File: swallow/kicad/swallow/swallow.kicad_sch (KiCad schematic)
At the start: 0 parts

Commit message: ++ - kamangir/bolt#746
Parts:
- added C1: 470 mF, symbol Device:C
- added D1: yellow, symbol Device:LED
- added D2: red, symbol Device:LED
- added D3: green, symbol Device:LED
- added D4: P6KE6.8A, Diode_SMD:D_SOD-523, symbol Diode:1N4148WT
- added D5, D6, D7, D8: blue, symbol Device:LED
- added J1: Raspberry_Pi_2_3, symbol Connector:Raspberry_Pi_2_3
- added J2: echo2, symbol Connector:Conn_01x01_Pin
- added J3: ground, symbol Connector_Generic:Conn_02x06_Top_Bottom
- added J4: VCC, symbol Connector_Generic:Conn_02x06_Top_Bottom
- added J5: echo3, symbol Connector:Conn_01x01_Pin
- added J6: echo4, symbol Connector:Conn_01x01_Pin
- added J7: echo1, symbol Connector:Conn_01x01_Pin
- added J8: power terminal, symbol Connector:Screw_Terminal_01x02
- added R1, R11, R14, R2, R3, R6, R8: 330 ohm, symbol Device:R
- added R10, R13, R5, R7: 3.3 kohm, symbol Device:R
- added R12, R15, R4, R9: 2.2 kohm, symbol Device:R
- added SW1: SW_Push, symbol Switch:SW_Push
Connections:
- new net: D6.1 (K), R8.1
- new net: C1.2, D1.1 (K), D2.1 (K), D3.1 (K), D4.1 (K), J1.14 (GND), J1.20 (GND), J1.25 (GND), J1.30 (GND), J1.34 (GND), J1.39 (GND), J1.6 (GND), J1.9 (GND), J3.1 (Pin_1), J3.10 (Pin_10), J3.11 (Pin_11), J3.12 (Pin_12), J3.2 (Pin_2), J3.3 (Pin_3), J3.4 (Pin_4), J3.5 (Pin_5), J3.6 (Pin_6), J3.7 (Pin_7), J3.8 (Pin_8), J3.9 (Pin_9), J8.1 (Pin_1), R10.2, R11.2, R13.2, R14.2, R5.2, R6.2, R7.2, R8.2, SW1.1
- new net: C1.1, D4.2 (A), J1.2 (5V), J1.4 (5V), J4.1 (Pin_1), J4.10 (Pin_10), J4.11 (Pin_11), J4.12 (Pin_12), J4.2 (Pin_2), J4.3 (Pin_3), J4.4 (Pin_4), J4.5 (Pin_5), J4.6 (Pin_6), J4.7 (Pin_7), J4.9 (Pin_9), J8.2 (Pin_2)
- new net: D6.2 (A), J1.38 (GPIO20/MOSI1), R7.1, R9.2
- new net: J7.1 (Pin_1), R15.1
- new net: D8.2 (A), J1.18 (GPIO24), R13.1, R15.2
- new net: D3.2 (A), R3.1
- new net: D8.1 (K), R14.1
- new net: J6.1 (Pin_1), R12.1
- new net: D7.2 (A), J1.40 (GPIO21/SCLK1), R10.1, R12.2
- new net: D7.1 (K), R11.1
- new net: D1.2 (A), R1.1
- new net: J1.11 (GPIO17), R1.2
- new net: J5.1 (Pin_1), R9.1
- new net: D5.2 (A), J1.22 (GPIO25), R4.2, R5.1
- new net: D2.2 (A), R2.1
- new net: D5.1 (K), R6.1
- new net: J1.13 (GPIO27), R3.2
- new net: J2.1 (Pin_1), R4.1
- new net: J1.15 (GPIO22), R2.2
- new net: J1.37 (GPIO26), SW1.2
- new net: J1.1 (3V3), J1.17 (3V3)

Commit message: ++ - kamangir/bolt#746
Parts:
- added J10: evens, symbol Connector:Conn_01x20_Pin
- added J9: odds, symbol Connector:Conn_01x20_Pin
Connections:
- net at J1.12 (GPIO18/PWM0): now also J10.6 (Pin_6)
- net at J1.16 (GPIO23): now also J10.8 (Pin_8)
- net at J1.29 (GCLK1/GPIO5): now also J9.15 (Pin_15)
- net at J1.31 (GCLK2/GPIO6): now also J9.16 (Pin_16)
- net at J1.32 (PWM0/GPIO12): now also J10.16 (Pin_16)
- net at J1.33 (PWM1/GPIO13): now also J9.17 (Pin_17)
- net at J1.35 (GPIO19/MISO1): now also J9.18 (Pin_18)
- net at J1.36 (GPIO16): now also J10.18 (Pin_18)
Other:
- moved on the sheet: C1, D4, J8

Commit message: ++ - kamangir/bolt#746
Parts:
- C1: value 470 mF -> 470 µF; footprint (none) -> Capacitor_THT:CP_Radial_D8.0mm_P3.50mm
- D1, D5, D6, D7, D8: footprint (none) -> LED_THT:LED_D5.0mm
- D2: renamed from D3; value green -> red; footprint (none) -> LED_THT:LED_D5.0mm
- D3: renamed from D2; value red -> green; footprint (none) -> LED_THT:LED_D5.0mm
- D4: footprint Diode_SMD:D_SOD-523 -> Diode_THT:D_DO-15_P10.16mm_Horizontal
- J1: footprint (none) -> Connector_PinHeader_2.54mm:PinHeader_2x20_P2.54mm_Vertical
- J10, J9: footprint (none) -> Connector_PinHeader_2.54mm:PinHeader_1x20_P2.54mm_Vertical
- J2, J5, J6, J7: footprint (none) -> Connector_PinHeader_2.54mm:PinHeader_1x01_P2.54mm_Vertical
- J3, J4: footprint (none) -> Connector_PinHeader_2.54mm:PinHeader_2x04_P2.54mm_Vertical
- J8: footprint (none) -> TerminalBlock:TerminalBlock_MaiXu_MX126-5.0-02P_1x02_P5.00mm
- R1, R10, R11, R12, R13, R14, R15, R4, R5, R6, R7, R8, R9: footprint (none) -> Resistor_THT:R_Axial_DIN0207_L6.3mm_D2.5mm_P10.16mm_Horizontal
- R2: renamed from R3; footprint (none) -> Resistor_THT:R_Axial_DIN0207_L6.3mm_D2.5mm_P10.16mm_Horizontal
- R3: renamed from R2; footprint (none) -> Resistor_THT:R_Axial_DIN0207_L6.3mm_D2.5mm_P10.16mm_Horizontal
- SW1: footprint (none) -> Button_Switch_THT:SW_PUSH_6mm
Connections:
- net at R8.1: now also D6.2 (A); no longer D6.1 (K)
- net at C1.2, D1.1 (K), D2.1 (K)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: now also D5.1 (K), D6.1 (K), D7.1 (K), D8.1 (K), J1.13 (GPIO27), J9.7 (Pin_7), R2.2; no longer R11.2, R14.2, R6.2, R8.2
- net at C1.1, D4.2 (A), J1.2 (5V)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: now also J1.11 (GPIO17), J4.8 (Pin_8), J9.6 (Pin_6), R1.2
- net at J1.38 (GPIO20/MOSI1), R7.1, R9.2: now also J10.19 (Pin_19), R8.2; no longer D6.2 (A)
- net at J9.19 (Pin_19): now also J1.37 (GPIO26), SW1.2
- net at J9.8 (Pin_8): now also J1.15 (GPIO22), R3.2
- net at J1.18 (GPIO24), R13.1, R15.2: now also J10.9 (Pin_9), R14.2; no longer D8.2 (A)
- net at R14.1: now also D8.2 (A); no longer D8.1 (K)
- net at J1.40 (GPIO21/SCLK1), R10.1, R12.2: now also J10.20 (Pin_20), R11.1; no longer D7.2 (A)
- net at J1.22 (GPIO25), R4.2, R5.1: now also J10.11 (Pin_11), R6.1; no longer D5.2 (A)
- new net: D7.2 (A), R11.2
- new net: D5.2 (A), R6.2
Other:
- moved on the sheet: D5, D6, D7, D8, J5, J6, R10, R11, R12, R14, R6, R7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

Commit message: ++ - kamangir/bolt#746
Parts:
- J1: footprint Connector_PinHeader_2.54mm:PinHeader_2x20_P2.54mm_Vertical -> Connector_PinSocket_2.54mm:PinSocket_2x20_P2.54mm_Vertical
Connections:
- net at C1.1, D4.2 (A), J1.2 (5V)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: now also J10.1 (Pin_1); no longer J1.11 (GPIO17), J9.6 (Pin_6), R1.2
- net at C1.2, D1.1 (K), D2.1 (K)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: now also J10.3 (Pin_3); no longer J1.13 (GPIO27), J9.7 (Pin_7), R2.2
- new net: J1.11 (GPIO17), J9.6 (Pin_6), R1.2
- new net: J1.13 (GPIO27), J9.7 (Pin_7), R2.2
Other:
- moved on the sheet: C1, D4
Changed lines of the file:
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@@
 	)
 	(junction
+		(at 200.66 43.18)
+		(diameter 0)
+		(color 0 0 0 0)
+	)
+	(junction
 		(at 140.97 134.62)
 		(diameter 0)
@@
 	)
 	(junction
-		(at 128.27 43.18)
+		(at 205.74 134.62)
 		(diameter 0)
 		(color 0 0 0 0)
 	)
 	(junction
-		(at 121.92 80.01)
+		(at 128.27 43.18)
 		(diameter 0)
 		(color 0 0 0 0)
 	)
 	(junction
-		(at 143.51 58.42)
+		(at 121.92 80.01)
 		(diameter 0)
 		(color 0 0 0 0)
@@
 	)
 	(junction
-		(at 143.51 66.04)
-		(diameter 0)
-		(color 0 0 0 0)
-	)
-	(junction
 		(at 177.8 43.18)
 		(diameter 0)
@@
 	(wire
 		(pts
-			(xy 128.27 64.77) (xy 128.27 80.01)
+			(xy 128.27 76.2) (xy 128.27 80.01)
 		)
 		(stroke
@@
 	(wire
 		(pts
-			(xy 128.27 43.18) (xy 128.27 57.15)
+			(xy 128.27 43.18) (xy 128.27 68.58)
 		)
 		(stroke
@@
 	(wire
 		(pts
-			(xy 143.51 66.04) (xy 39.37 66.04)
-		)
-		(stroke
-			(width 0)
-			(type default)
-		)
-	)
-	(wire
-		(pts
 			(xy 46.99 49.53) (xy 46.99 114.3)
 		)
@@
 	(wire
 		(pts
-			(xy 143.51 58.42) (xy 38.1 58.42)
-		)
-		(stroke
-			(width 0)
-			(type default)
-		)
-	)
-	(wire
-		(pts
 			(xy 140.97 157.48) (xy 140.97 134.62)
 		)
@@
 	(wire
 		(pts
+			(xy 251.46 72.39) (xy 251.46 43.18)
+		)
+		(stroke
+			(width 0)
+			(type default)
+		)
+	)
+	(wire
+		(pts
 			(xy 71.12 80.01) (xy 76.2 80.01)
 		)
@@
 	(wire
 		(pts
-			(xy 175.26 58.42) (xy 143.51 58.42)
+			(xy 38.1 58.42) (xy 175.26 58.42)
 		)
 		(stroke
@@
 	(wire
 		(pts
+			(xy 246.38 134.62) (xy 205.74 134.62)
+		)
+		(stroke
+			(width 0)
+			(type default)
+		)
+	)
+	(wire
+		(pts
 			(xy 119.38 67.31) (xy 41.91 67.31)
 		)
@@
 	(wire
 		(pts
+			(xy 262.89 77.47) (xy 246.38 77.47)
+		)
+		(stroke
+			(width 0)
+			(type default)
+		)
+	)
+	(wire
+		(pts
 			(xy 121.92 91.44) (xy 121.92 97.79)
 		)
@@
 	(wire
 		(pts
-			(xy 143.51 66.04) (xy 143.51 80.01)
+			(xy 143.51 77.47) (xy 143.51 80.01)
 		)
 		(stroke
@@
 	(wire
 		(pts
-			(xy 173.99 66.04) (xy 143.51 66.04)
+			(xy 246.38 77.47) (xy 246.38 134.62)
+		)
+		(stroke
+			(width 0)
+			(type default)
+		)
+	)
+	(wire
+		(pts
+			(xy 39.37 66.04) (xy 173.99 66.04)
 		)
 		(stroke
@@
 	(wire
 		(pts
+			(xy 262.89 72.39) (xy 251.46 72.39)
+		)
+		(stroke
+			(width 0)
+			(type default)
+		)
+	)
+	(wire
+		(pts
 			(xy 185.42 102.87) (xy 144.78 102.87)
 		)
@@
 	(wire
 		(pts
-			(xy 143.51 43.18) (xy 143.51 58.42)
+			(xy 143.51 43.18) (xy 143.51 69.85)
 		)
 		(stroke
@@
 	(wire
 		(pts
+			(xy 251.46 43.18) (xy 200.66 43.18)
+		)
+		(stroke
+			(width 0)
+			(type default)
+		)
+	)
+	(wire
+		(pts
 			(xy 176.53 114.3) (xy 132.08 114.3)
 		)
@@
 		)
 	)
-	(label "2025-10-09"
-		(at 205.74 194.31 0)
-		(effects
-			(font
-				(size 1.27 1.27)
-			)
-			(justify left bottom)
-		)
-	)
 	(label "swallow shield"
 		(at 186.69 190.5 0)
@@
 		)
 	)
-	(label "v3"
+	(label "v4"
 		(at 267.97 194.31 0)
 		(effects
@@
 	(symbol
 		(lib_id "Diode:1N4148WT")
-		(at 143.51 62.23 90)
+		(at 143.51 73.66 90)
 		(unit 1)
 		(exclude_from_sim no)
@@
 		(fields_autoplaced yes)
 		(property "Reference" "D4"
-			(at 146.05 60.9599 90)
+			(at 146.05 72.3899 90)
 			(effects
 				(font
@@
 		)
 		(property "Value" "P6KE6.8A"
-			(at 146.05 63.4999 90)
+			(at 146.05 74.9299 90)
 			(effects
 				(font
@@
 		)
 		(property "Footprint" "Diode_THT:D_DO-15_P10.16mm_Horizontal"
-			(at 147.955 62.23 0)
+			(at 147.955 73.66 0)
 			(effects
 				(font
@@
 		)
 		(property "Datasheet" "https://www.diodes.com/assets/Datasheets/ds30396.pdf"
-			(at 143.51 62.23 0)
+			(at 143.51 73.66 0)
 			(effects
 				(font
@@
 		)
 		(property "Description" "75V 0.15A Fast switching Diode, SOD-523"
-			(at 143.51 62.23 0)
+			(at 143.51 73.66 0)
 			(effects
 				(font
@@
 		)
 		(property "Sim.Device" "D"
-			(at 143.51 62.23 0)
+			(at 143.51 73.66 0)
 			(effects
 				(font
@@
 		)
 		(property "Sim.Pins" "1=K 2=A"
-			(at 143.51 62.23 0)
+			(at 143.51 73.66 0)
 			(effects
 				(font
@@
 	(symbol
 		(lib_id "Device:C")
-		(at 128.27 60.96 0)
+		(at 128.27 72.39 0)
 		(unit 1)
 		(exclude_from_sim no)
@@
 		(fields_autoplaced yes)
 		(property "Reference" "C1"
-			(at 132.08 59.6899 0)
+			(at 132.08 71.1199 0)
 			(effects
 				(font
@@
 		)
 		(property "Value" "470 µF"
-			(at 132.08 62.2299 0)
+			(at 132.08 73.6599 0)
 			(effects
 				(font
@@
 		)
 		(property "Footprint" "Capacitor_THT:CP_Radial_D8.0mm_P3.50mm"
-			(at 129.2352 64.77 0)
+			(at 129.2352 76.2 0)
 			(effects
 				(font
@@
 		)
 		(property "Datasheet" "~"
-			(at 128.27 60.96 0)
+			(at 128.27 72.39 0)
 			(effects
 				(font
@@
 		)
 		(property "Description" "Unpolarized capacitor"
-			(at 128.27 60.96 0)
+			(at 128.27 72.39 0)
 			(effects
 				(font
@@
 			)
 		)
-		(property "Footprint" "Connector_PinHeader_2.54mm:PinHeader_2x20_P2.54mm_Vertical"
+		(property "Footprint" "Connector_PinSocket_2.54mm:PinSocket_2x20_P2.54mm_Vertical"
 			(at 205.74 92.71 0)
 			(effects

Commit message: ++ - kamangir/bolt#746
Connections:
- net at C1.1, J1.2 (5V), J1.4 (5V)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: now also D4.1 (K); no longer D4.2 (A)
- net at C1.2, D1.1 (K), D2.1 (K)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: now also D4.2 (A), J9.13 (Pin_13); no longer D4.1 (K)
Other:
- moved on the sheet: D4
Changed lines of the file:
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@@
+	)
+	(junction
+		(at 137.16 134.62)
+		(diameter 0)
+		(color 0 0 0 0)
 	)
 	(junction
@@
 	(wire
 		(pts
+			(xy 35.56 106.68) (xy 44.45 106.68)
+		)
+		(stroke
+			(width 0)
+			(type default)
+		)
+	)
+	(wire
+		(pts
 			(xy 251.46 132.08) (xy 251.46 97.79)
 		)
@@
 	(wire
 		(pts
+			(xy 44.45 177.8) (xy 137.16 177.8)
+		)
+		(stroke
+			(width 0)
+			(type default)
+		)
+	)
+	(wire
+		(pts
 			(xy 106.68 148.59) (xy 121.92 148.59)
 		)
@@
 	(wire
 		(pts
+			(xy 44.45 106.68) (xy 44.45 177.8)
+		)
+		(stroke
+			(width 0)
+			(type default)
+		)
+	)
+	(wire
+		(pts
 			(xy 140.97 157.48) (xy 140.97 134.62)
 		)
@@
 	(wire
 		(pts
-			(xy 121.92 134.62) (xy 140.97 134.62)
+			(xy 121.92 134.62) (xy 137.16 134.62)
 		)
 		(stroke
@@
 	(wire
 		(pts
+			(xy 137.16 134.62) (xy 140.97 134.62)
+		)
+		(stroke
+			(width 0)
+			(type default)
+		)
+	)
+	(wire
+		(pts
 			(xy 41.91 93.98) (xy 35.56 93.98)
+		)
+		(stroke
+			(width 0)
+			(type default)
+		)
+	)
+	(wire
+		(pts
+			(xy 137.16 177.8) (xy 137.16 134.62)
 		)
 		(stroke
@@
 	(symbol
 		(lib_id "Diode:1N4148WT")
-		(at 143.51 73.66 90)
+		(at 143.51 73.66 270)
 		(unit 1)
 		(exclude_from_sim no)
@@
 					(size 1.27 1.27)
 				)
-				(justify right)
+				(justify left)
 			)
 		)
@@
 					(size 1.27 1.27)
 				)
-				(justify right)
+				(justify left)
 			)
 		)
 		(property "Footprint" "Diode_THT:D_DO-15_P10.16mm_Horizontal"
-			(at 147.955 73.66 0)
-			(effects
-				(font
+			(at 139.065 73.66 0)
+			(effects
+				(font

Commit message: ++ - kamangir/bolt#746
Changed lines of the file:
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@@
 		)
 	)
-	(label "v4"
+	(label "v14"
 		(at 267.97 194.31 0)
 		(effects

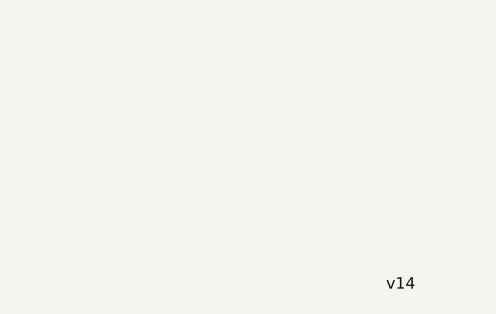
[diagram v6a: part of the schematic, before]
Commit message: fix - kamangir/bolt#746
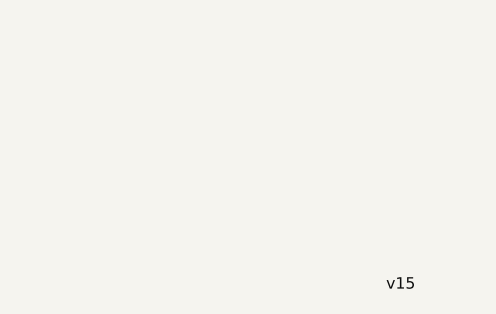
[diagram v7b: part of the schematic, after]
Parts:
- J3, J4: footprint Connector_PinHeader_2.54mm:PinHeader_2x04_P2.54mm_Vertical -> Connector_PinHeader_2.54mm:PinHeader_2x06_P2.54mm_Vertical
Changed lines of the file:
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@@
 		)
 	)
-	(label "v14"
+	(label "v15"
 		(at 267.97 194.31 0)
 		(effects
@@
 			)
 		)
-		(property "Footprint" "Connector_PinHeader_2.54mm:PinHeader_2x04_P2.54mm_Vertical"
+		(property "Footprint" "Connector_PinHeader_2.54mm:PinHeader_2x06_P2.54mm_Vertical"
 			(at 158.75 27.94 0)
 			(effects
@@
 			)
 		)
-		(property "Footprint" "Connector_PinHeader_2.54mm:PinHeader_2x04_P2.54mm_Vertical"
+		(property "Footprint" "Connector_PinHeader_2.54mm:PinHeader_2x06_P2.54mm_Vertical"
 			(at 161.29 149.86 0)
 			(effects

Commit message: ++ - kamangir/bolt#746
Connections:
- net pin2: now reaches C1.1, D4.1 (K), J1.2 (5V), J1.4 (5V), J10.1 (Pin_1), J4.1 (Pin_1), J4.10 (Pin_10), J4.11 (Pin_11), J4.12 (Pin_12), J4.2 (Pin_2), J4.3 (Pin_3), J4.4 (Pin_4), J4.5 (Pin_5), J4.6 (Pin_6), J4.7 (Pin_7), J4.8 (Pin_8), J4.9 (Pin_9), J8.2 (Pin_2)
- net pin2: now also J10.2 (Pin_2)
- net pin14: now reaches C1.2, D1.1 (K), D2.1 (K), D3.1 (K), D4.2 (A), D5.1 (K), D6.1 (K), D7.1 (K), D8.1 (K), J1.14 (GND), J1.20 (GND), J1.25 (GND), J1.30 (GND), J1.34 (GND), J1.39 (GND), J1.6 (GND), J1.9 (GND), J10.3 (Pin_3), J3.1 (Pin_1), J3.10 (Pin_10), J3.11 (Pin_11), J3.12 (Pin_12), J3.2 (Pin_2), J3.3 (Pin_3), J3.4 (Pin_4), J3.5 (Pin_5), J3.6 (Pin_6), J3.7 (Pin_7), J3.8 (Pin_8), J3.9 (Pin_9), J8.1 (Pin_1), J9.13 (Pin_13), R10.2, R13.2, R5.2, R7.2, SW1.1
- net pin14: now also J10.10 (Pin_10), J10.15 (Pin_15), J10.17 (Pin_17), J10.7 (Pin_7), J9.20 (Pin_20), J9.5 (Pin_5)
- net pin1: now reaches J9.1 (Pin_1)
- net pin1: now also J1.1 (3V3), J1.17 (3V3), J9.9 (Pin_9)
- net pin19: now reaches J9.10 (Pin_10)
- net pin19: now also J1.19 (MOSI0/GPIO10)
- net pin21: now reaches J9.11 (Pin_11)
- net pin21: now also J1.21 (MISO0/GPIO9)
- net pin23: now reaches J9.12 (Pin_12)
- net pin23: now also J1.23 (SCLK0/GPIO11)
- net pin27: now reaches J9.14 (Pin_14)
- net pin27: now also J1.27 (ID_SD/GPIO0)
- net pin3: now reaches J9.2 (Pin_2)
- net pin3: now also J1.3 (SDA/GPIO2)
- net pin5: now reaches J9.3 (Pin_3)
- net pin5: now also J1.5 (SCL/GPIO3)
- net pin7: now reaches J9.4 (Pin_4)
- net pin7: now also J1.7 (GCLK0/GPIO4)
- net pin24: now reaches J10.12 (Pin_12)
- net pin24: now also J1.24 (~{CE0}/GPIO8)
- net pin26: now reaches J10.13 (Pin_13)
- net pin26: now also J1.26 (~{CE1}/GPIO7)
- net pin28: now reaches J10.14 (Pin_14)
- net pin28: now also J1.28 (ID_SC/GPIO1)
- net pin8: now reaches J10.4 (Pin_4)
- net pin8: now also J1.8 (GPIO14/TXD)
- net pin10: now reaches J10.5 (Pin_5)
- net pin10: now also J1.10 (GPIO15/RXD)
